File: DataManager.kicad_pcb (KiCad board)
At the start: 2 copper layers, 74 x 38 mm, 37 parts, among them J1 Micro_SD_Card, J2 6P6C, J3 USB_B_Micro, J4 8P8C, J5 8P8C, Q1 MMBT3904, Q2 MMBT3904, U1 ESP32-WROOM-32D, U2 SI8621AB-B-ISR, U3 AP2210-3.3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

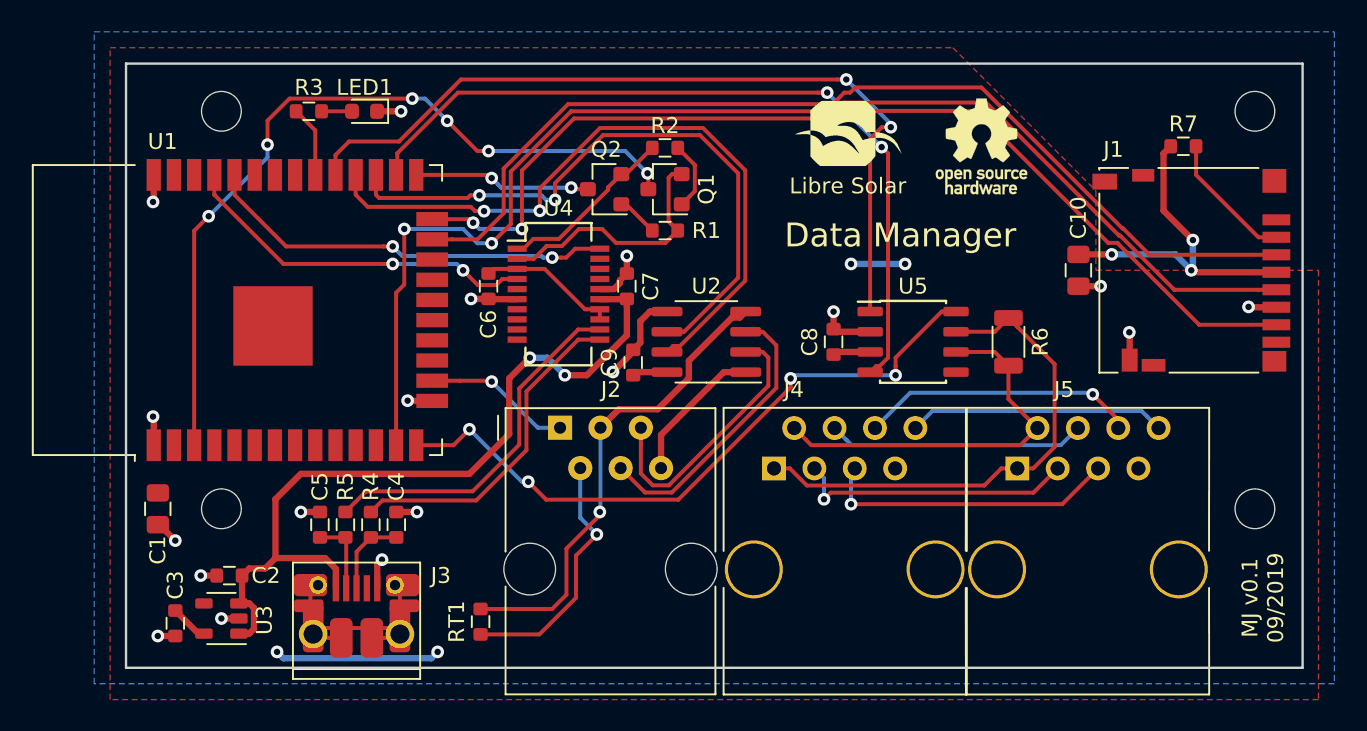
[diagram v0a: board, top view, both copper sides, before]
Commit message: Board v0.2: Errors fixed
- Pull-up resistor on reset pin
- LS.one (serial) pinout fixed (reversed)
- Isolator U2 RX/TX pinout fixed
- PCB mounting hole diameter enlarged to 3 mm
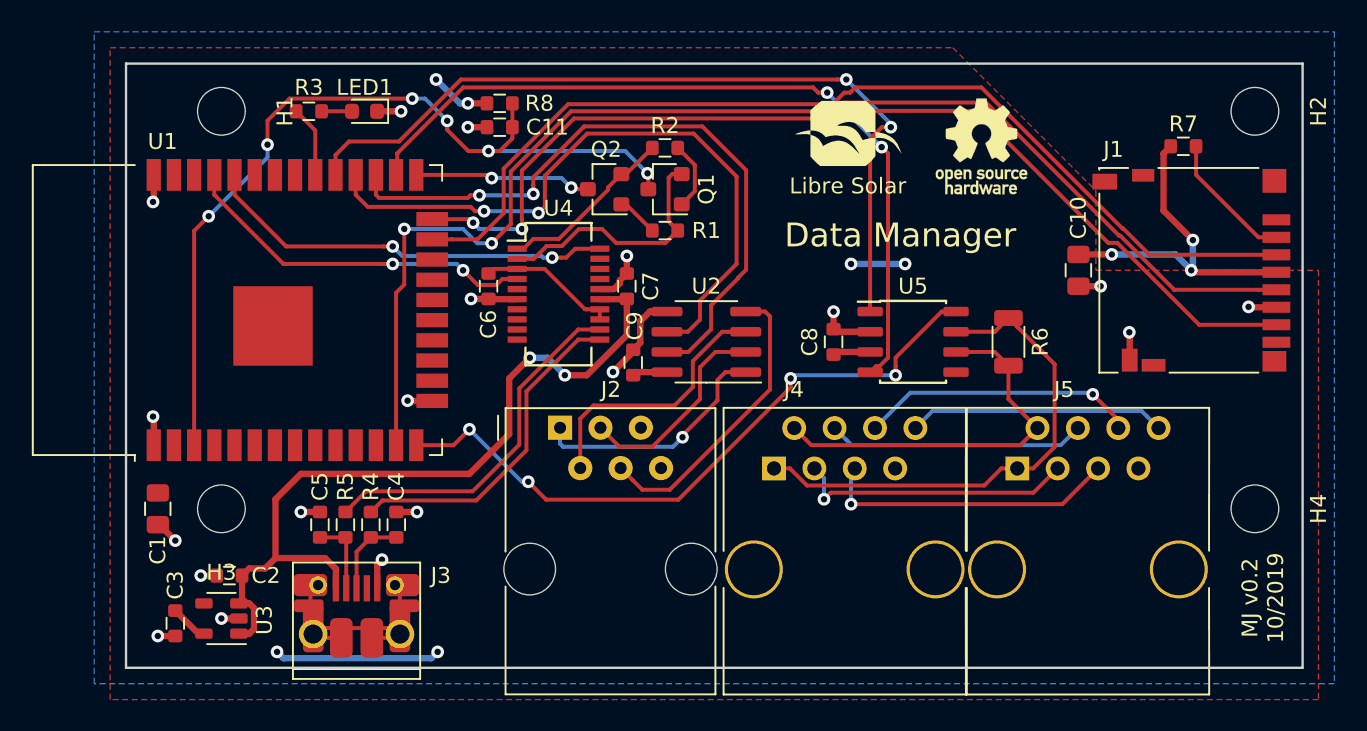
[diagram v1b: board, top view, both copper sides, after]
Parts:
- removed RT1: R_NTC, LibreSolar:R_0603_1608
- added C11: 2.2u, LibreSolar:C_0603_1608, F.Cu at (153.5, 81.0)
- added R8: 10k, LibreSolar:R_0603_1608, F.Cu at (153.5, 79.5)
- C2: value 1u -> 2.2u
- H1, H2, H3, H4: footprint MountingHole:MountingHole_2.5mm -> MountingHole:MountingHole_3mm
- R4, R5: value 1k -> 27
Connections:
- J2 pad 1: /BTN -> /VCC_EXT
- J2 pad 2: /TSENSE -> /RX_EXT
- J2 pad 3: /GND_EXT -> /TX_EXT
- J2 pad 4: /TX_EXT -> /GND_EXT
- J2 pad 5: /RX_EXT -> Net-(J2-Pad5)
- J2 pad 6: /VCC_EXT -> Net-(J2-Pad6)
- U1 pad 16: /BTN -> Net-(U1-Pad16)
- U2 pad 2: /RX_EXT -> /TX_EXT
- U2 pad 3: /TX_EXT -> /RX_EXT
- U2 pad 6: /U2_RX -> /U2_TX
- U2 pad 7: /U2_TX -> /U2_RX
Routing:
- net /TSENSE: track 16.1 -> 0.00 mm, vias 1 -> 0
- net /GND_EXT: track 30.0 -> 18.8 mm, vias 1 -> 0
- net /BTN: track 9.27 -> 0.00 mm, vias 1 -> 0
- net /VCC_EXT: track 9.05 -> 15.5 mm, vias 0 -> 1
- net /TX_EXT: track 18.1 -> 13.3 mm
- net /RESET: track 49.8 -> 54.1 mm
- net +3V3: track 42.5 -> 46.3 mm, vias 7 -> 9
- net /U2_RX: track 40.1 -> 42.5 mm
- net /U2_TX: track 44.0 -> 42.4 mm
- net GND: track 36.2 -> 37.4 mm, vias 18 -> 19
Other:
- board text added: "MJ v0.2 10/2019"
- board text removed: "MJ v0.1 09/2019"
